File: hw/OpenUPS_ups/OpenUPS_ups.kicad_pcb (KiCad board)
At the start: 4 copper layers, 90 x 62 mm, 283 parts, among them J1001 USB4105-GF-A, J101 Barrel Jack, J102 XT30PW-M, J103 XT30PW-M, J104 S2B-PH-K_1x02, J105 S2B-PH-K_1x02, J106 Screw Terminal, J107 Screw Terminal, J108 Screw Terminal, J109 JST XH, J110 JST XH, J501 Conn_01x03, J701 0022053031, J702 0022053031, J901 Qwiic, J902 Qwiic, Q1001 2N7002, Q301 AON7534, Q302 AON7534, Q303 AON7534, Q304 AON7534, Q401 2N7002, Q402 AON7534, Q403 AON7534, Q404 AON7534, Q405 AON7534, Q601 AON7534, Q602 AON7534, Q603 AON7534, Q604 AON7534, Q701 2N7002, Q702 2N7002, U1001 MCP6547, U1002 AP22814BW5, U1003 NUP2301MW6T1G, U101 AVR32DB48x-xPT, U102 NUP2301MW6T1G, U103 LM75BTP,147, U201 TPS51397A, U202 INA180A3, U301 NCP81599, U401 NCP431, U402 BD99950, U403 MCP6001R, U404 DZDH0401DW, U405 INA180A1, U601 NCP81599, U701 NUP2301MW6T1G, U702 NUP2301MW6T1G, U801 AP7383-33W5, U901 π220N31

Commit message: Layout WIP
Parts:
- removed R409: 10m 1/2W, Resistor_SMD:R_1206_3216Metric
- added Q406: AON7423, footprints:DFN 3x3 MOSFET, F.Cu at (261.8, 90.8)
- R424: value 10m 1/2W -> 20m 1/2W
- moved C301 168.3 mm to (107.5, 15.5)
- moved C302 168.3 mm to (107.5, 13.0)
- moved C601 168.3 mm to (69.2, 13.0)
- moved C602 168.3 mm to (73.2, 14.0)
- moved R302 168.3 mm to (103.5, 13.0)
- moved R304 168.3 mm to (99.5, 13.0)
- moved R306 168.3 mm to (99.5, 15.0)
- moved R601 168.3 mm to (69.2, 14.5)
- moved R602 168.3 mm to (71.7, 14.0)
- moved R604 168.3 mm to (78.1, 14.0)
- moved R606 168.3 mm to (76.6, 14.0)
- moved R301 168.3 mm to (103.5, 15.5)
- moved R704 157.4 mm to (93.8, 27.5), turned to 90 degrees
- moved R703 156.3 mm to (91.2, 27.5), turned to 90 degrees
- moved R702 155.3 mm to (88.7, 27.5), turned to 90 degrees
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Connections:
- net /Aux Power Supplies/EN2 renamed Vin
- R424 pad 1: Net-(R409-Pad1) -> Net-(C411-Pad1)
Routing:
- net /Ext. I2C Interface/XI2C_GND: track 0.00 -> 35.0 mm, vias 0 -> 2
- net /Ext. I2C Interface/XI2C_VCC: track 0.00 -> 31.6 mm, vias 0 -> 2
- net /Ext. I2C Interface/XI2C_SCL: track 0.00 -> 28.9 mm, vias 0 -> 2
- net /Ext. I2C Interface/XI2C_SDA: track 0.00 -> 28.7 mm, vias 0 -> 2
- net Net-(J702-Pin_2): track 0.00 -> 15.2 mm
- net /F_Tach1: track 0.00 -> 11.8 mm
- net /B_RX: track 0.00 -> 8.89 mm
- net GND: track 53.4 -> 61.3 mm, vias 81 -> 89
- net Net-(J701-Pin_2): track 0.00 -> 7.55 mm
- net /B_TX: track 0.00 -> 6.43 mm
- net +3.3VA: track 1.54 -> 4.72 mm, vias 2 -> 4
- net +12V: track 22.7 -> 24.8 mm
- net /I2C_E_SDA: track 0.00 -> 1.90 mm
- net /I2C_E_SCL: track 0.00 -> 1.90 mm
- net /F_Tach0: track 0.00 -> 1.71 mm

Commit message: PCB placement
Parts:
- moved R416 100.2 mm to (149.5, 88.0), turned to -90 degrees
- moved R417 98.0 mm to (151.8, 88.0), turned to -90 degrees
- moved L401 97.9 mm to (151.5, 97.0), turned to 90 degrees
- moved Q404 96.0 mm to (147.2, 104.2)
- moved Q405 90.3 mm to (155.0, 88.5), turned to 180 degrees
- moved C411 89.0 mm to (151.5, 104.8), turned to 180 degrees
- moved C416 85.8 mm to (162.5, 94.0), turned to -90 degrees
- moved C405 85.0 mm to (151.5, 107.2), turned to 180 degrees
- moved Q403 83.9 mm to (155.8, 104.2)
- moved R424 79.8 mm to (156.2, 107.2)
- moved Q402 77.5 mm to (160.0, 118.5), turned to 180 degrees
- moved C210 58.7 mm to (138.1, 77.0), turned to 0 degrees
- moved C414 55.9 mm to (199.2, 76.0), turned to 90 degrees
- moved R415 54.3 mm to (200.8, 76.0), turned to 90 degrees
- moved Q406 53.2 mm to (209.0, 83.8), turned to 90 degrees
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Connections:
- C207 pad 1: Net-(C205-Pad2) -> +5V
- C208 pad 1: Net-(C205-Pad2) -> +5V
- C210 pad 1: Net-(C205-Pad2) -> +5V
- C211 pad 1: Net-(C205-Pad2) -> +5V
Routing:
- net Net-(Q1001-D): track 0.00 -> 34.8 mm
- net +5V: track 3.34 -> 29.5 mm, vias 0 -> 7
- net Net-(J1001-CC2): track 0.00 -> 23.1 mm, vias 0 -> 2
- net Net-(J1001-CC1): track 0.00 -> 19.4 mm
- net Net-(U1002-OUT): track 0.00 -> 16.3 mm
- net Net-(U1001A--): track 0.00 -> 16.2 mm
- net GND: track 61.3 -> 74.1 mm, vias 89 -> 94
- net Net-(U202-+): track 0.00 -> 6.18 mm
- net Net-(U202--): track 0.00 -> 3.33 mm
- net +3.3VA: track 4.72 -> 7.30 mm, vias 4 -> 5
- net Net-(C305-Pad2): track 0.11 -> 1.63 mm
- net /USB_FORCE: track 0.00 -> 1.21 mm, vias 0 -> 1
- net Net-(J701-Pin_2): track 7.55 -> 6.86 mm
- net Net-(C205-Pad2): track 3.34 -> 2.84 mm
- added copper zone on F.Cu, net +5V
- added copper zone on In2.Cu, net +5V
- added copper zone on B.Cu, net GND
- added copper zone on In1.Cu, net GND

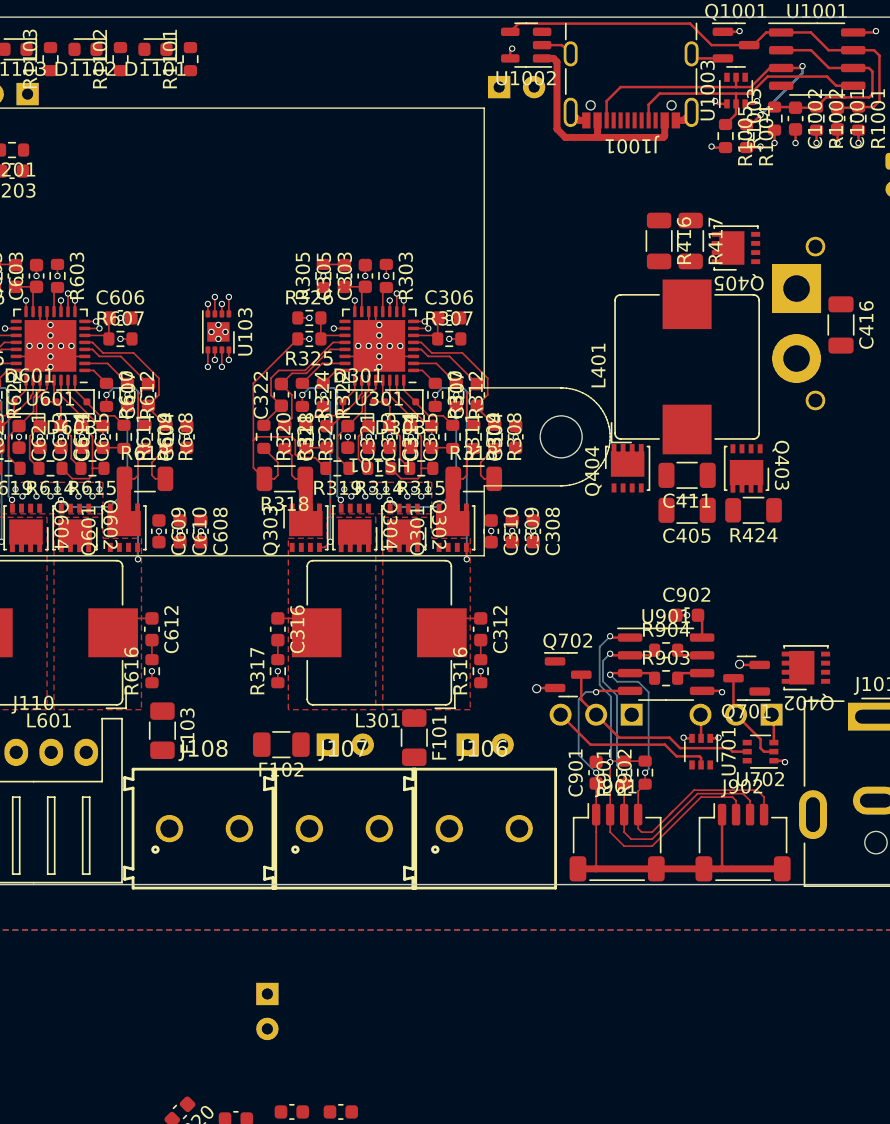
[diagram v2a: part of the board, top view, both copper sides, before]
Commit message: Extra large transistor copper pours
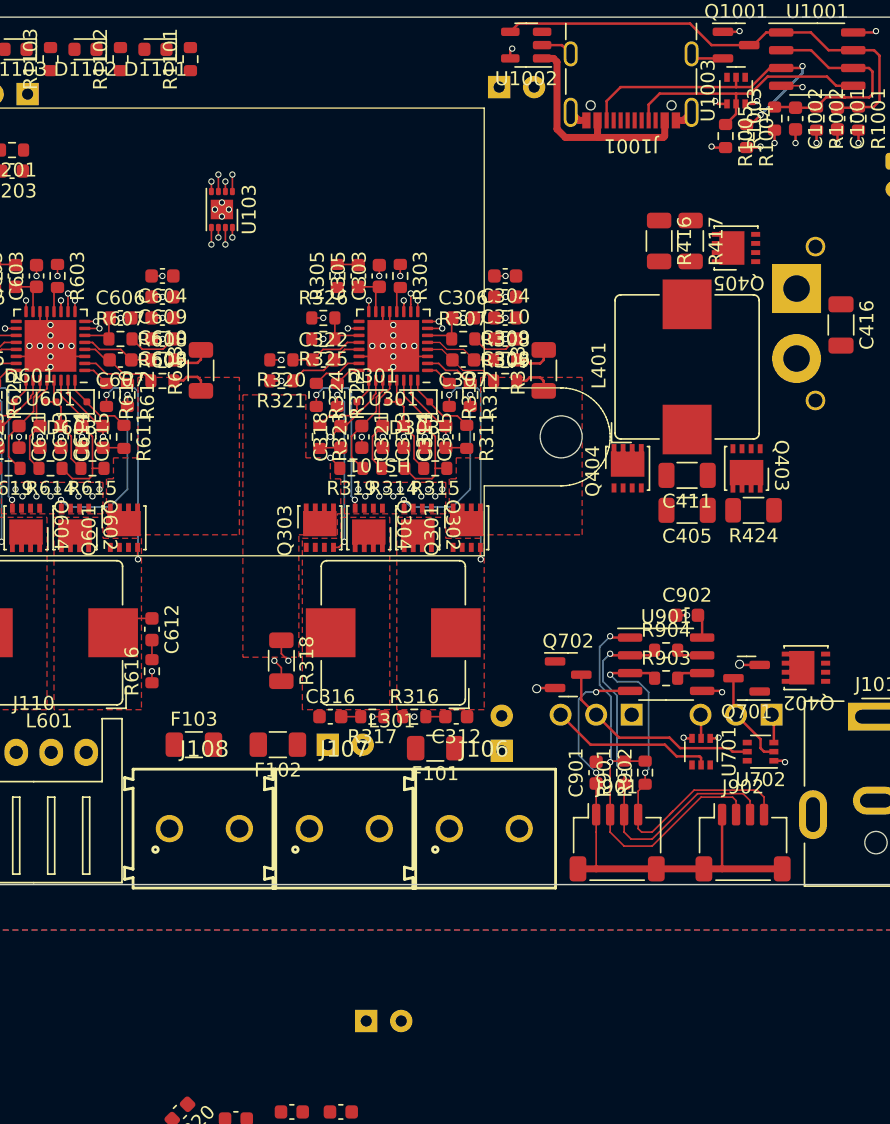
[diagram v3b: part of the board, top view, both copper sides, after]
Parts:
- moved C310 16.8 mm to (138.5, 92.0), turned to 180 degrees
- moved C609 16.8 mm to (114.0, 92.0), turned to 180 degrees
- moved C610 15.3 mm to (114.0, 93.5), turned to 180 degrees
- moved C309 15.3 mm to (138.5, 93.5), turned to 180 degrees
- moved C608 14.0 mm to (114.0, 95.0), turned to 180 degrees
- moved C308 13.9 mm to (138.5, 95.0), turned to 180 degrees
- moved R318 13.0 mm to (122.5, 118.0), turned to -90 degrees
- moved C604 11.6 mm to (114.0, 90.5), turned to 180 degrees
- moved C304 11.5 mm to (138.5, 90.5), turned to 180 degrees
- moved R313 9.22 mm to (141.2, 97.2), turned to 90 degrees
- moved U103 8.75 mm to (118.2, 85.8)
- moved R613 8.72 mm to (116.8, 97.2), turned to 90 degrees
- moved R317 7.49 mm to (129.0, 122.0), turned to 180 degrees
- moved C324 7.33 mm to (128.6, 143.8), turned to 0 degrees
- moved C316 7.29 mm to (126.0, 122.0), turned to 0 degrees
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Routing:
- net +AdjV: track 22.7 -> 4.35 mm, vias 1 -> 4
- net Net-(U601B-CSP1): track 10.6 -> 5.24 mm
- net Net-(U301B-CSP1): track 10.6 -> 5.24 mm
- net Net-(U301C-CSN2): track 10.5 -> 5.24 mm
- net Vsys: track 8.46 -> 12.8 mm, vias 2 -> 0
- net Net-(Q303-D-Pad5): track 6.41 -> 2.49 mm, vias 0 -> 2
- net Net-(Q601-D-Pad5): track 6.41 -> 2.84 mm
- net Net-(Q301-D-Pad5): track 6.41 -> 2.84 mm
- net Net-(U301C-CSP2): track 9.04 -> 5.66 mm
- net Net-(U301B-CSN1): track 9.03 -> 5.66 mm
- net Net-(U601B-CSN1): track 9.03 -> 5.66 mm
- net Net-(U301B-VSW1): track 8.41 -> 5.21 mm
- net Net-(U301C-VSW2): track 7.96 -> 5.84 mm, vias 0 -> 1
- net GND: track 74.1 -> 75.6 mm, vias 94 -> 95
- added copper zone on F.Cu, net Net-(Q301-D-Pad5)
- added copper zone on F.Cu, net Net-(Q303-D-Pad5)
- added copper zone on F.Cu, net Net-(Q601-D-Pad5)

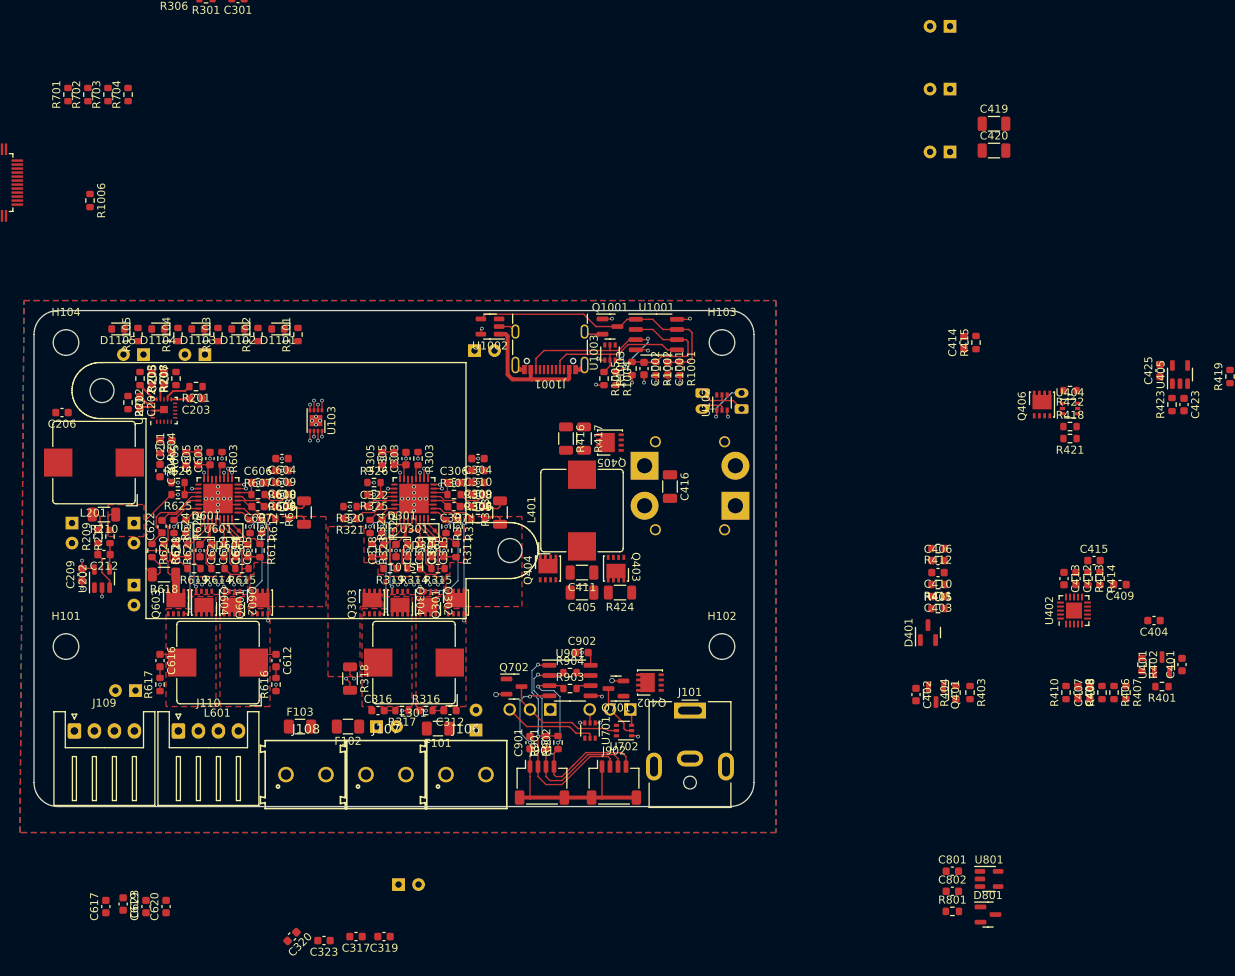
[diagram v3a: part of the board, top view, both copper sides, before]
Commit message: Charger layout
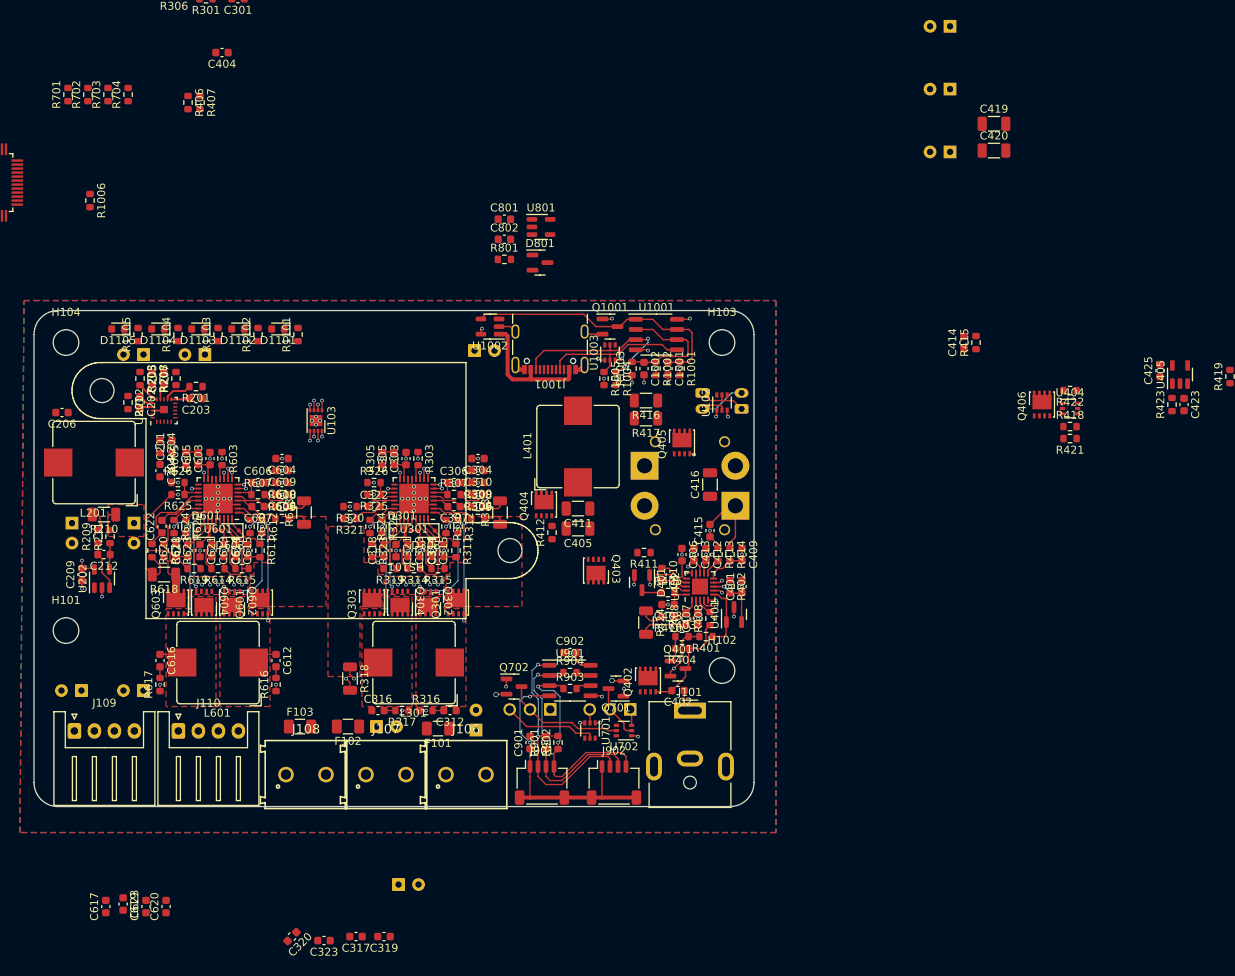
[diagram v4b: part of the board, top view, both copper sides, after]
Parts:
- moved R406 137.2 mm to (102.2, 46.0)
- moved R407 137.2 mm to (103.8, 46.0)
- moved C404 136.4 mm to (106.5, 39.8)
- moved C801 98.9 mm to (141.8, 60.6)
- moved U801 98.9 mm to (146.4, 61.5)
- moved C802 98.9 mm to (141.8, 63.1)
- moved D801 98.9 mm to (146.2, 66.0)
- moved R801 98.9 mm to (141.8, 65.6)
- moved R401 57.3 mm to (167.0, 112.8)
- moved C401 55.9 mm to (171.5, 106.5)
- moved U401 53.9 mm to (170.5, 110.0)
- moved R402 52.4 mm to (170.0, 106.5)
- moved R410 50.6 mm to (162.2, 110.2), turned to 180 degrees
- moved C407 49.9 mm to (166.0, 110.5)
- moved C408 49.9 mm to (164.5, 110.5), turned to 90 degrees
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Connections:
- C411 pad 1: Net-(C411-Pad1) -> /Aux Power Supplies/EN2
- D801 pad 1: Vin -> /Aux Power Supplies/EN2
- Q403 pad 5: Net-(C411-Pad1) -> /Aux Power Supplies/EN2
- Q403 pad 6: Net-(C411-Pad1) -> /Aux Power Supplies/EN2
- Q403 pad 7: Net-(C411-Pad1) -> /Aux Power Supplies/EN2
- Q403 pad 8: Net-(C411-Pad1) -> /Aux Power Supplies/EN2
- R410 pad 2: Net-(C411-Pad1) -> /Aux Power Supplies/EN2
- R424 pad 1: Net-(C411-Pad1) -> /Aux Power Supplies/EN2
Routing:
- net Net-(U401-K): track 0.00 -> 14.1 mm
- net Net-(Q401-D): track 0.00 -> 13.0 mm
- net Vin: track 0.00 -> 11.4 mm, vias 0 -> 2
- net Net-(U402-ACP): track 0.00 -> 9.74 mm
- net +BATT: track 0.00 -> 9.69 mm
- net GND: track 75.6 -> 85.0 mm, vias 95 -> 104
- net +5V: track 29.5 -> 23.2 mm
- net Net-(U402-BATT): track 0.00 -> 5.33 mm
- net Net-(U402-HDRV): track 0.00 -> 4.43 mm
- net Vsys: track 12.8 -> 16.9 mm, vias 0 -> 2
- net Net-(U402-BOOT): track 0.00 -> 3.80 mm
- net Net-(U402-ACN): track 0.00 -> 3.59 mm
- net Net-(U402-PHASE): track 0.00 -> 3.57 mm
- net Net-(Q401-G): track 0.00 -> 3.30 mm
- net Net-(U402-VCC): track 0.00 -> 3.16 mm
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
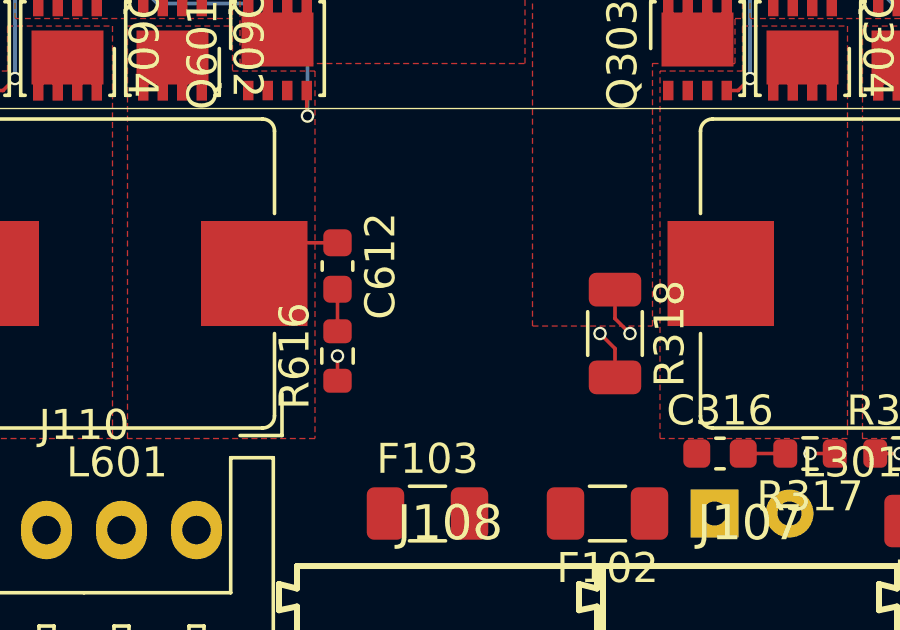
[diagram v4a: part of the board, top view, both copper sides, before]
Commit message: Added the fifth mounting hole
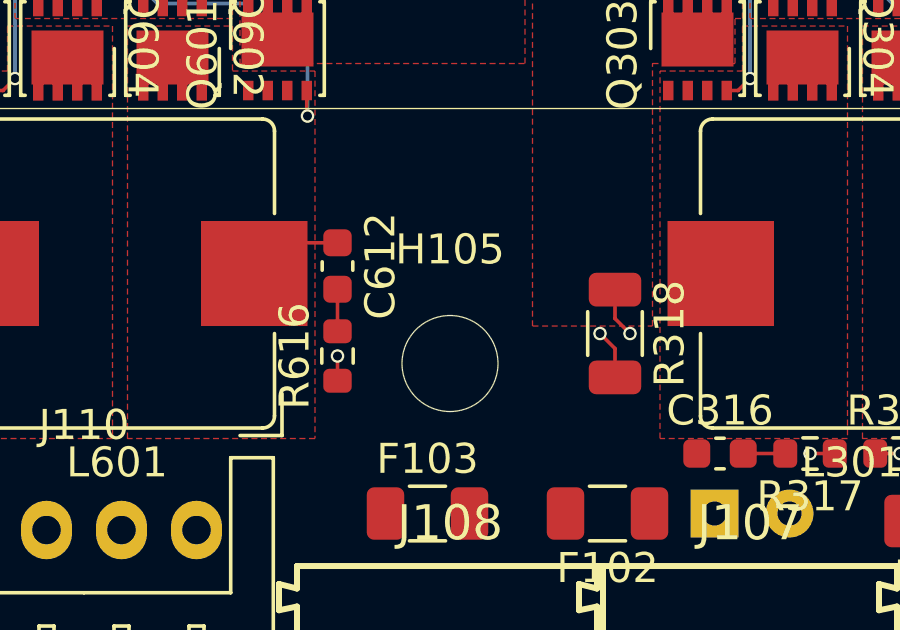
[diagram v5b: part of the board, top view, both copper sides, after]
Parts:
- added H105: MountingHole, MountingHole:MountingHole_3.2mm_M3_DIN965, F.Cu at (117.0, 119.0)
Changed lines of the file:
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@@
     )
+  )
+  (footprint "MountingHole:MountingHole_3.2mm_M3_DIN965" locked (layer "F.Cu")
+    (at 117 119)
+    (descr "Mounting Hole 3.2mm, no annular, M3, DIN965")
+    (tags "mounting hole 3.2mm no annular m3 din965")
+    (property "Sheetfile" "OpenUPS_ups.kicad_sch")
+    (property "Sheetname" "")
+    (property "ki_description" "Mounting Hole without connection")
+    (property "ki_keywords" "mounting hole")
+    (attr exclude_from_pos_files)
+    (fp_text reference "H105" (at 0 -3.8) (layer "F.SilkS")
+        (effects (font (size 1 1) (thickness 0.15)))
+    )
+    (fp_text value "MountingHole" (at 0 3.8) (layer "F.Fab")
+        (effects (font (size 1 1) (thickness 0.15)))
+    )
+    (fp_text user "${REFERENCE}" (at 0 0) (layer "F.Fab")
+        (effects (font (size 1 1) (thickness 0.15)))
+    )
+    (fp_circle (center 0 0) (end 2.8 0)
+      (stroke (width 0.15) (type solid)) (fill none) (layer "Cmts.User"))
+    (fp_circle (center 0 0) (end 3.05 0)
+      (stroke (width 0.05) (type solid)) (fill none) (layer "F.CrtYd"))
+    (pad "" np_thru_hole circle locked (at 0 0) (size 3.2 3.2) (drill 3.2) (layers "*.Cu" "*.Mask"))
   )
   (footprint "Resistor_SMD:R_1206_3216Metric" (layer "F.Cu")

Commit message: More charger layout
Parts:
- moved C419 67.0 mm to (146.8, 85.0), turned to 180 degrees
- moved C420 66.4 mm to (146.8, 87.2), turned to 180 degrees
- moved C414 35.3 mm to (197.0, 111.2)
- moved R415 35.3 mm to (198.5, 111.2)
- moved C405 13.2 mm to (148.5, 112.2)
- moved C411 12.7 mm to (148.5, 109.2)
- moved Q404 9.06 mm to (152.5, 103.2)
- moved R412 8.28 mm to (155.0, 103.8), turned to -90 degrees
- moved U101 7.70 mm to (78.5, 48.5), turned to 90 degrees
- moved D401 7.22 mm to (160.8, 113.0)
- moved Q403 5.88 mm to (159.0, 103.2)
- moved C902 5.62 mm to (155.2, 116.8), turned to 180 degrees
- moved L401 5.02 mm to (151.5, 94.0)
- moved R416 3.69 mm to (156.2, 85.0)
- moved R417 3.69 mm to (156.2, 87.2)
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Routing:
- net Net-(U402-PHASE): track 3.57 -> 24.7 mm
- net Net-(U402-ACP): track 9.74 -> 26.3 mm
- net /Aux Power Supplies/EN2: track 3.05 -> 18.6 mm
- net Net-(U402-LDRV): track 0.78 -> 11.5 mm, vias 1 -> 2
- net Vin: track 11.4 -> 21.8 mm, vias 2 -> 1
- net GND: track 85.0 -> 91.1 mm, vias 104 -> 119
- net Net-(U402-HDRV): track 4.43 -> 10.4 mm, vias 0 -> 2
- net Net-(D401-Pad3): track 2.55 -> 8.13 mm, vias 0 -> 2
- net Net-(Q404-G): track 0.00 -> 1.56 mm
- net Net-(Q403-G): track 0.00 -> 1.56 mm
- net Vsys: track 16.9 -> 15.7 mm, vias 2 -> 1
- net +3.3VA: track 9.07 -> 8.07 mm
- added copper zone on F.Cu, net Vin
